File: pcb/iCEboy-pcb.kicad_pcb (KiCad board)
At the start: 2 copper layers, 51 x 61 mm, 65 parts, among them J1 DMG-CardEdge, J2 PROG_PORT, Q1 2N7002K, U1 TC74LCXR163245FT, U2 TC74LCXR163245FT, U3 ICE40UP5K-SG48ITR, U4 TPS79901DDCR, U5 TPS79901DDCR, U6 W25Q80DVSSIG, X1 SG-210STF 20MHz

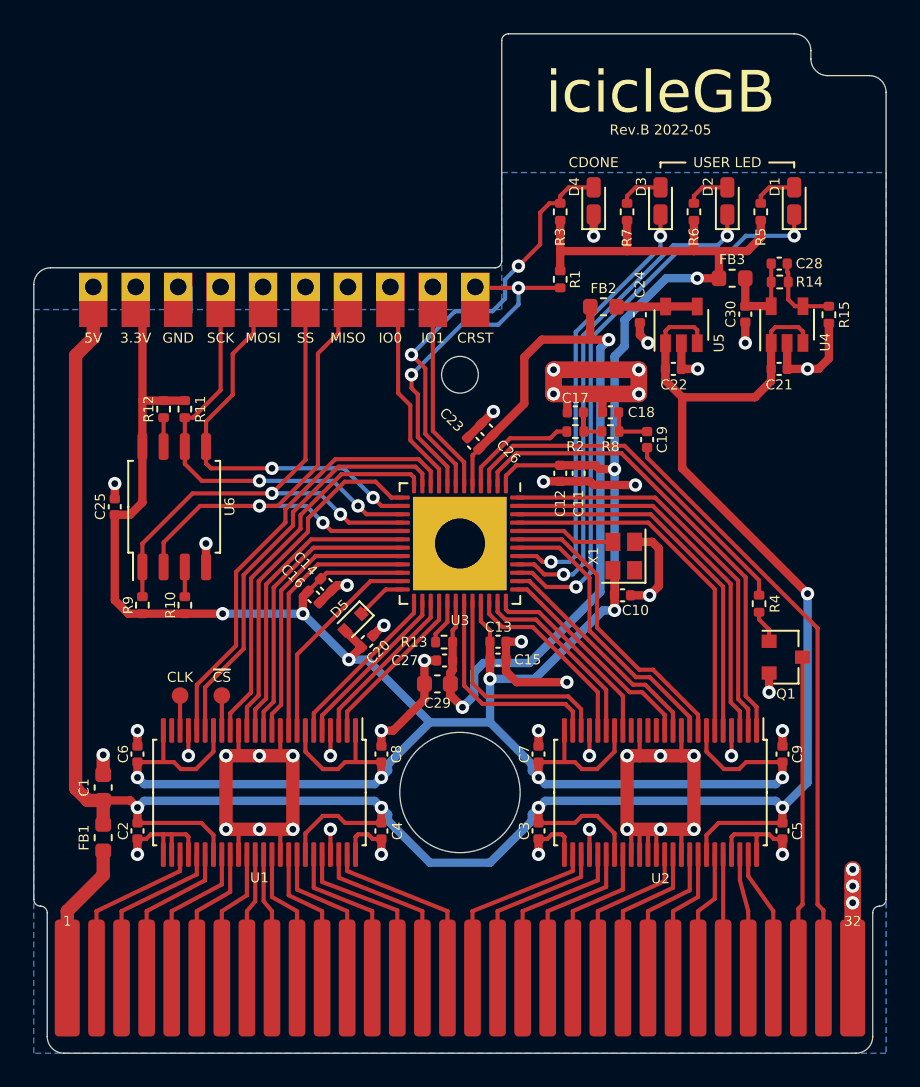
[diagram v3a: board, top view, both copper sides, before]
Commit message: add mounting hole
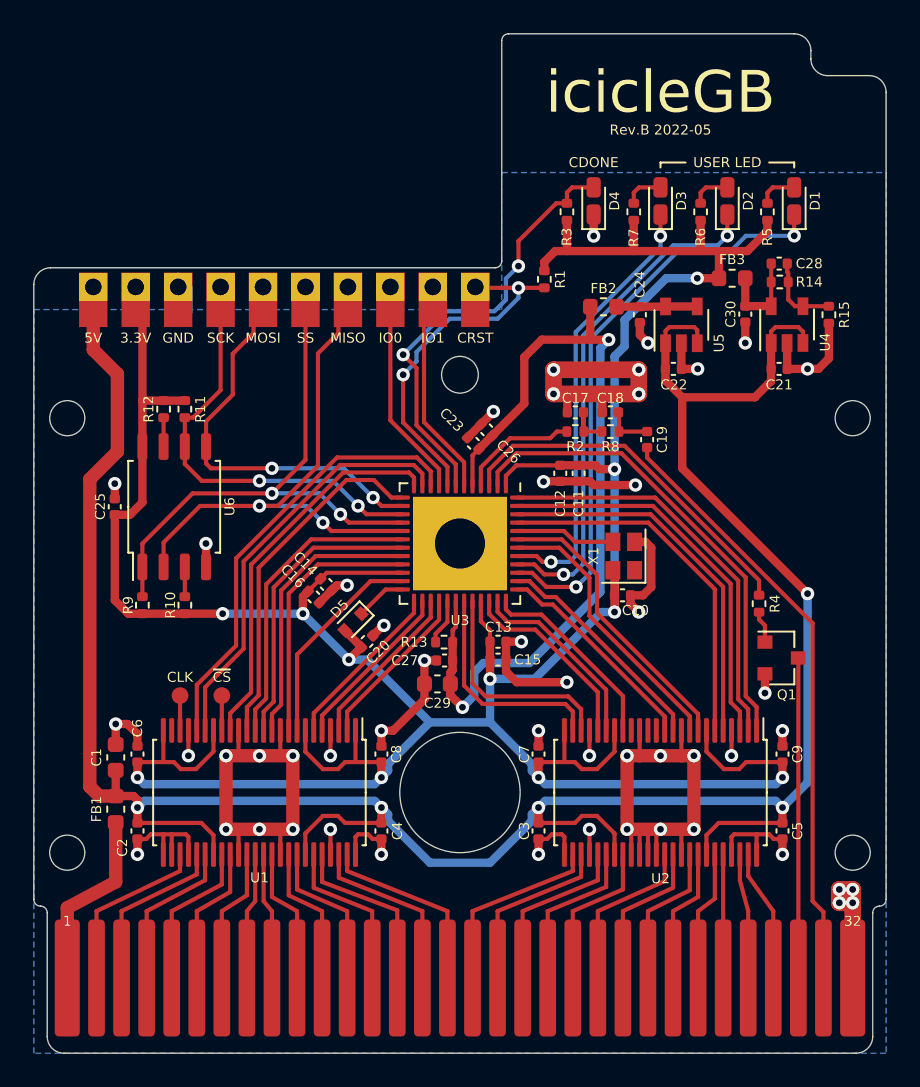
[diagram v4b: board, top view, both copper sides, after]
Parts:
- added H1: MH_2mm, MountingHole:MountingHole_2.1mm, F.Cu at (36.5, 83.5)
- added H2: MH_2mm, MountingHole:MountingHole_2.1mm, F.Cu at (83.5, 83.5)
- added H3: MH_2mm, MountingHole:MountingHole_2.1mm, F.Cu at (36.5, 57.5)
- added H4: MH_2mm, MountingHole:MountingHole_2.1mm, F.Cu at (83.5, 57.5)
- moved C1 1.95 mm to (39.4, 77.8)
- moved FB1 1.86 mm to (39.4, 80.9)
- moved R1 0.95 mm to (65.0, 49.2)
- moved R3 0.40 mm to (66.4, 45.1)
- moved R5 0.40 mm to (78.4, 45.1)
- moved R6 0.40 mm to (74.4, 45.1)
- moved R7 0.40 mm to (70.4, 45.1)
- moved Q1 0.25 mm to (79.2, 71.8)
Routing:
- net GND: track 156.2 -> 159.2 mm
- net /VCC: track 8.50 -> 11.1 mm
- net +3V3: track 203.3 -> 204.2 mm
- net /CDONE: track 26.1 -> 26.7 mm
- net /IO0: track 11.7 -> 12.3 mm

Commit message: update illustration
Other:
- board text removed: "TODO add board information silk"
- board text removed: "icicleGB"

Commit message: add reverse current protection circuit between VCC and 5V, remove mounthole
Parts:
- removed the FB1 at (39.4, 80.9)
- removed H1, H2, H3, H4: MH_2mm, MountingHole:MountingHole_2.1mm
- added Q1: DMG3415U, Package_TO_SOT_SMD:SOT-23, F.Cu at (40.4, 72.8)
- added Q2: HN4A56JU, Package_TO_SOT_SMD:SOT-353_SC-70-5, F.Cu at (40.4, 69.3)
- added R1: 12kΩ, Resistor_SMD:R_0402_1005Metric, F.Cu at (43.1, 68.7)
- added R2: DNP, Resistor_SMD:R_0603_1608Metric, F.Cu at (39.3, 78.2)
- added R3: 12kΩ, Resistor_SMD:R_0402_1005Metric, F.Cu at (43.1, 70.0)
- moved C1 3.78 mm to (39.3, 81.6), turned to -90 degrees
- moved C25 2.53 mm to (40.1, 60.4), turned to -90 degrees
- moved R14 2.53 mm to (44.3, 54.6)
- moved U6 2.53 mm to (43.7, 60.4)
- moved R15 2.53 mm to (43.1, 54.6)
- moved R12 2.53 mm to (41.8, 66.3)
- moved R13 2.53 mm to (44.3, 66.3)
- moved Q3 0.43 mm to (78.8, 71.7), turned to 90 degrees
- moved FB2 0.12 mm to (76.3, 49.0)
- moved R16 0.10 mm to (79.1, 49.2)
- moved C26 0.06 mm to (79.1, 48.2)
- renumbered C21 to C20, C22 to C21, C20 to C22, C24 to C23, C23 to C24, C28 to C26, C26 to C27, C27 to C28, C30 to C29, C29 to C30, FB2 to FB1, FB3 to FB2, Q1 to Q3, R7 to R10, R8 to R11, R9 to R12, R10 to R13, R11 to R14, R12 to R15, R14 to R16, R15 to R17, R13 to R18, R1 to R4, R2 to R5, R3 to R6, R4 to R7, R5 to R8, R6 to R9
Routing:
- net /VCC: track 11.1 -> 25.5 mm
- net Net-(Q2-Pad2): track 0.00 -> 6.13 mm
- net GND: track 159.2 -> 162.9 mm, vias 51 -> 52
- net Net-(Q1-Pad1): track 0.00 -> 3.20 mm
- net +5V: track 153.6 -> 156.8 mm, vias 5 -> 6
- net /SPI-SS: track 33.1 -> 31.0 mm
- net /SPI-MISO: track 31.7 -> 29.8 mm
- net +3V3: track 204.2 -> 205.9 mm
- net /CB-~{RST}: track 19.2 -> 20.8 mm
- net /SPI-SCK: track 25.3 -> 23.6 mm
- net Net-(Q3-Pad1): track 1.93 -> 3.53 mm
- net /SPI-MOSI: track 23.2 -> 21.6 mm
